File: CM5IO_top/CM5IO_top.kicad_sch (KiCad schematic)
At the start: 26 parts, among them J1 USB_C_Receptacle_USB2.0, J10 J_DShot600_FC, J3 J_PSU_EN, J7 J_FC_UART, J8 THD-20-R, J9 J_DShot600_ESC, U2 AP7361C-33E, U3 AP7361C-33E

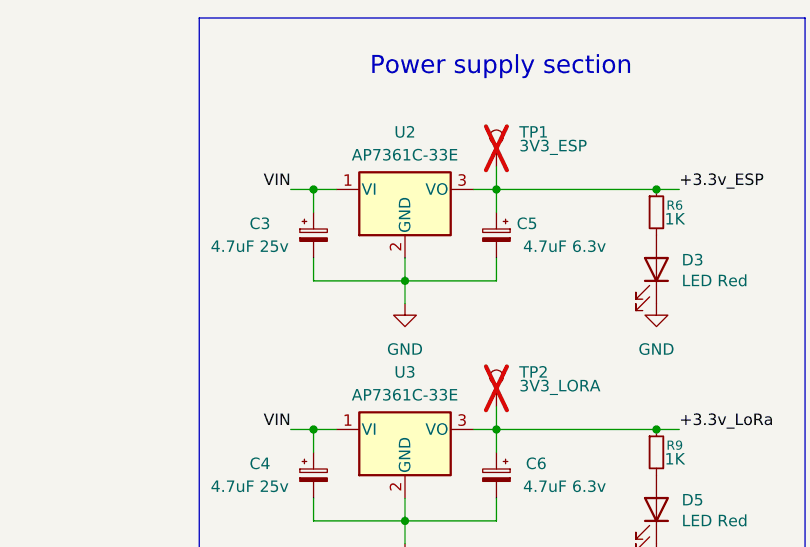
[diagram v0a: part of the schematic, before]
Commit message: redesigning upper board
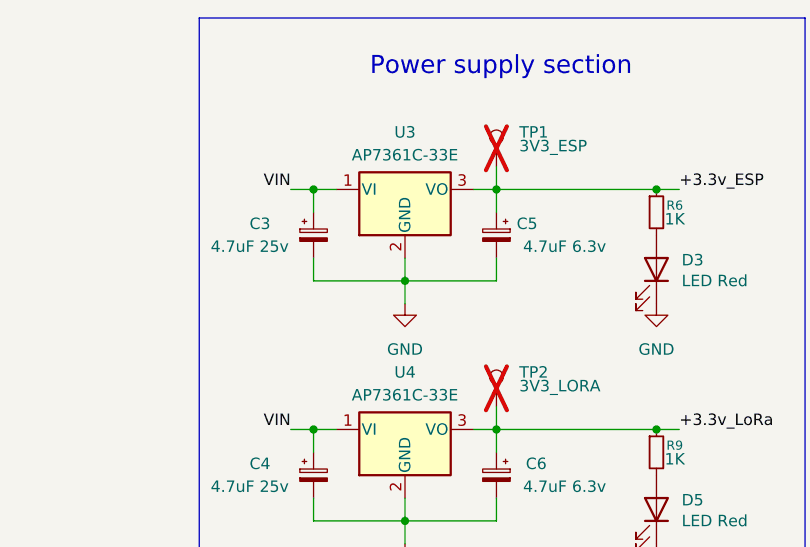
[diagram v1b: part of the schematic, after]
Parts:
- renumbered U2 to U3, U3 to U4
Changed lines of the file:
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@@
 		(dnp no)
 		(fields_autoplaced yes)
-		(property "Reference" "U3"
+		(property "Reference" "U4"
 			(at 236.22 55.88 0)
 			(effects
@@
 			(project "CM5IO_top"
 				(path "/45032d28-0209-4e67-a308-47ee4cd3805e"
-					(reference "U3")
+					(reference "U4")
 					(unit 1)
 				)
@@
 		(dnp no)
 		(fields_autoplaced yes)
-		(property "Reference" "U2"
+		(property "Reference" "U3"
 			(at 236.22 29.21 0)
 			(effects
@@
 			(project ""
 				(path "/45032d28-0209-4e67-a308-47ee4cd3805e"
-					(reference "U2")
-					(unit 1)
-				)
+					(reference "U3")
+					(unit 1)
+				)

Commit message: upper board finished (I hope)
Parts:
- C3, C4: value 4.7uF 25v -> 4.7uF 35v
- C5, C6: value 4.7uF 6.3v -> 4.7uF 10v
- J3: footprint Connector_PinHeader_2.54mm:PinHeader_1x02_P2.54mm_Vertical_SMD_Pin1Left -> Connector_PinSocket_2.54mm:PinSocket_1x02_P2.54mm_Vertical_SMD_Pin1Left
- J8: footprint Connector_PinHeader_2.54mm:PinHeader_2x20_P2.54mm_Vertical -> Connector_PinSocket_2.54mm:PinSocket_2x20_P2.54mm_Vertical
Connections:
- net +5v_RPi: now also J8.2 (Pin_2), J8.4 (Pin_4); no longer J8.1 (Pin_1), J8.3 (Pin_3)
- net GND: now also J8.14 (Pin_14), J8.20 (Pin_20), J8.25 (Pin_25), J8.30 (Pin_30), J8.34 (Pin_34), J8.39 (Pin_39), J8.6 (Pin_6), J8.9 (Pin_9); no longer J8.10 (Pin_10), J8.13 (Pin_13), J8.19 (Pin_19), J8.26 (Pin_26), J8.29 (Pin_29), J8.33 (Pin_33), J8.40 (Pin_40), J8.5 (Pin_5)
- net GPIO10: now also J8.19 (Pin_19); no longer J8.20 (Pin_20)
- net GPIO11: now also J8.23 (Pin_23); no longer J8.24 (Pin_24)
- net GPIO12: now also J8.32 (Pin_32); no longer J8.31 (Pin_31)
- net GPIO13: now also J8.33 (Pin_33); no longer J8.34 (Pin_34)
- net GPIO14_UART_TX: now also J8.8 (Pin_8); no longer J8.7 (Pin_7)
- net GPIO15_UART_RX: now also J8.10 (Pin_10); no longer J8.9 (Pin_9)
- net GPIO16: now also J8.36 (Pin_36); no longer J8.35 (Pin_35)
- net GPIO17: now also J8.11 (Pin_11); no longer J8.12 (Pin_12)
- net GPIO18: now also J8.12 (Pin_12); no longer J8.11 (Pin_11)
- net GPIO19: now also J8.35 (Pin_35); no longer J8.36 (Pin_36)
- net GPIO2: now also J8.3 (Pin_3); no longer J8.4 (Pin_4)
- net GPIO20: now also J8.38 (Pin_38); no longer J8.37 (Pin_37)
- net GPIO21: now also J8.40 (Pin_40); no longer J8.39 (Pin_39)
- net GPIO22: now also J8.15 (Pin_15); no longer J8.16 (Pin_16)
- net GPIO23: now also J8.16 (Pin_16); no longer J8.15 (Pin_15)
- net GPIO24: now also J8.18 (Pin_18); no longer J8.17 (Pin_17)
- net GPIO25: now also J8.22 (Pin_22); no longer J8.21 (Pin_21)
- net GPIO26: now also J8.37 (Pin_37); no longer J8.38 (Pin_38)
- net GPIO27: now also J8.13 (Pin_13); no longer J8.14 (Pin_14)
- net GPIO3: now also J8.5 (Pin_5); no longer J8.6 (Pin_6)
- net GPIO4: now also J8.7 (Pin_7); no longer J8.8 (Pin_8)
- net GPIO5: now also J8.29 (Pin_29); no longer J8.30 (Pin_30)
- net GPIO6: now also J8.31 (Pin_31); no longer J8.32 (Pin_32)
- net GPIO7: now also J8.26 (Pin_26); no longer J8.25 (Pin_25)
- net GPIO8: now also J8.24 (Pin_24); no longer J8.23 (Pin_23)
- net GPIO9: now also J8.21 (Pin_21); no longer J8.22 (Pin_22)
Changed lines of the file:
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@@
 	(symbol
 		(lib_id "Connector_Generic:Conn_02x20_Odd_Even")
-		(at 38.1 62.23 0)
-		(mirror y)
+		(at 35.56 62.23 0)
 		(unit 1)
 		(exclude_from_sim no)
@@
 		(dnp no)
 		(property "Reference" "J8"
-			(at 29.21 36.83 0)
+			(at 44.45 36.83 0)
 			(effects
 				(font
@@
 			)
 		)
-		(property "Footprint" "Connector_PinHeader_2.54mm:PinHeader_2x20_P2.54mm_Vertical"
-			(at 38.1 62.23 0)
+		(property "Footprint" "Connector_PinSocket_2.54mm:PinSocket_2x20_P2.54mm_Vertical"
+			(at 35.56 62.23 0)
 			(effects
 				(font
@@
 		)
 		(property "Datasheet" "https://www.toby.co.uk/uploads/publications/1673.pdf"
-			(at 38.1 62.23 0)
+			(at 35.56 62.23 0)
 			(effects
 				(font
@@
 		)
 		(property "Description" ""
-			(at 38.1 62.23 0)
+			(at 35.56 62.23 0)
 			(effects
 				(font
@@
 		)
 		(property "Field4" "Toby"
-			(at 38.1 62.23 0)
+			(at 35.56 62.23 0)
 			(effects
 				(font
@@
 		)
 		(property "Field5" "THD-20-R"
-			(at 38.1 62.23 0)
+			(at 35.56 62.23 0)
 			(effects
 				(font
@@
 		)
 		(property "Field6" "THD-20-R"
-			(at 38.1 62.23 0)
+			(at 35.56 62.23 0)
 			(effects
 				(font
@@
 		)
 		(property "Field7" "Toby"
-			(at 38.1 62.23 0)
+			(at 35.56 62.23 0)
 			(effects
 				(font
@@
 		)
 		(property "Field8" "UCON00511"
-			(at 38.1 62.23 0)
+			(at 35.56 62.23 0)
 			(effects
 				(font
@@
 		)
 		(property "Part Description" "PinHeader_2x20_P2.54mm_Vertical"
-			(at 38.1 62.23 0)
+			(at 35.56 62.23 0)
 			(effects
 				(font
@@
 			)
 		)
-		(property "Footprint" "Connector_PinHeader_2.54mm:PinHeader_1x02_P2.54mm_Vertical_SMD_Pin1Left"
+		(property "Footprint" "Connector_PinSocket_2.54mm:PinSocket_1x02_P2.54mm_Vertical_SMD_Pin1Left"
 			(at 40.64 29.21 0)
 			(effects
@@
 			)
 		)
-		(property "Value" "4.7uF 25v"
+		(property "Value" "4.7uF 35v"
 			(at 214.63 68.58 0)
 			(effects
@@
 			)
 		)
-		(property "Value" "4.7uF 25v"
+		(property "Value" "4.7uF 35v"
 			(at 214.63 41.91 0)
 			(effects
@@
 		(dnp no)
 		(property "Reference" "C6"
-			(at 251.968 66.04 0)
-			(effects
-				(font
-					(size 1.27 1.27)
-				)
-				(justify left)
-			)
-		)
-		(property "Value" "4.7uF 6.3v"
-			(at 258.572 68.58 0)
+			(at 251.206 66.04 0)
+			(effects
+				(font
+					(size 1.27 1.27)
+				)
+				(justify left)
+			)
+		)
+		(property "Value" "4.7uF 10v"
+			(at 258.318 68.072 0)
 			(effects
 				(font
@@
 			)
 		)
-		(property "Value" "4.7uF 6.3v"
-			(at 258.572 41.91 0)
-			(effects
-				(font
+		(property "Value" "4.7uF 10v"
+			(at 258.064 41.656 0)
+			(effects
+				(font
